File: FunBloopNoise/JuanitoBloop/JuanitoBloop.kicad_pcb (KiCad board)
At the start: 2 copper layers, 30 parts, among them J1 Trig, J2 CV, J3 Out, Q1 2N3904, Q2 2N3904, U1 NE555, U2 4046, U3 NE5532

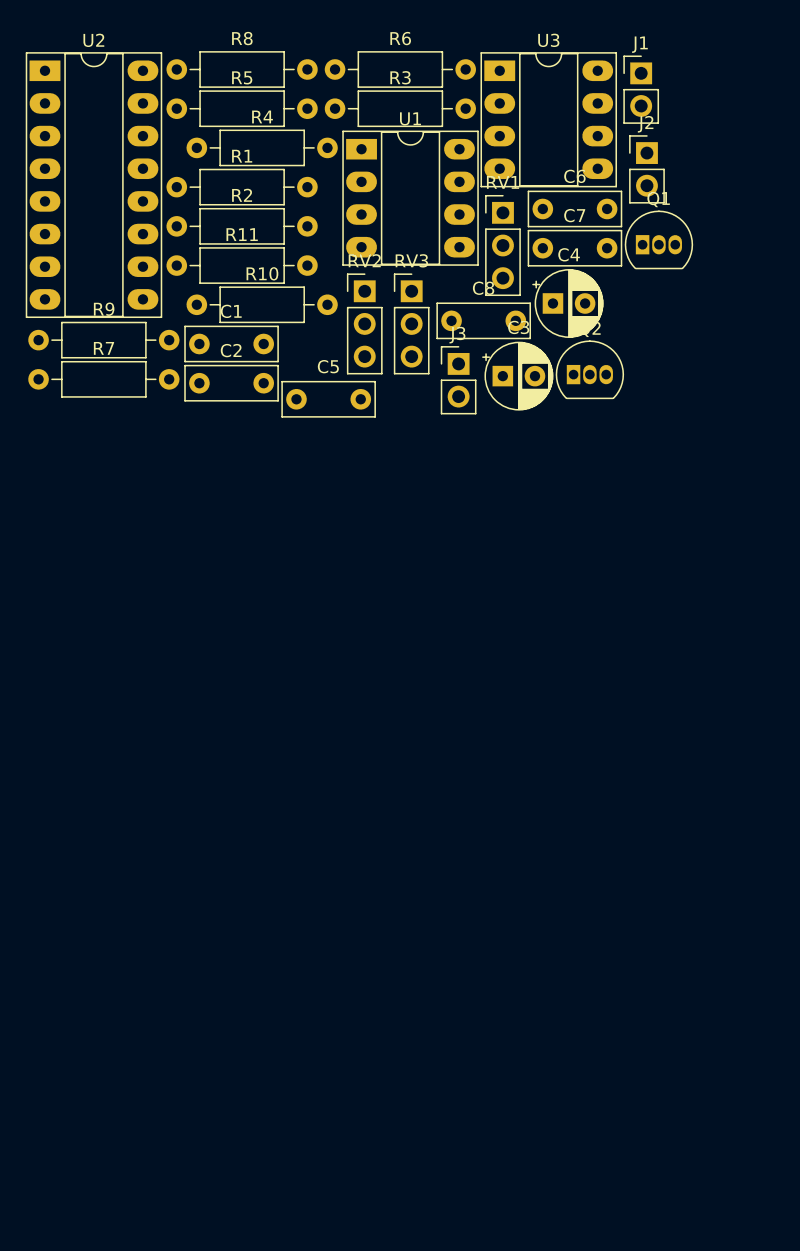
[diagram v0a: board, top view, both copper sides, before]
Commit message: schematic v2 and pcb v1
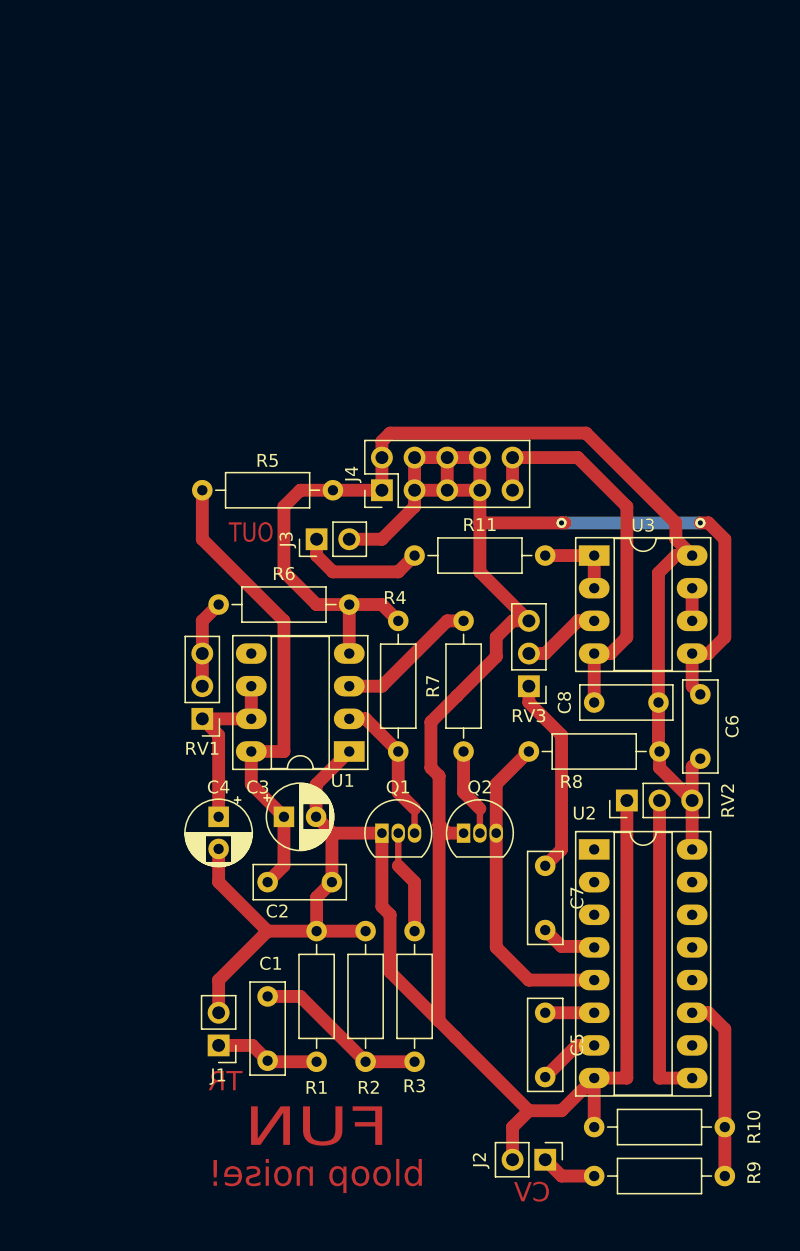
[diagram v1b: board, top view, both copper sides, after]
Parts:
- added J4: Power, Connector_PinHeader_2.54mm:PinHeader_2x05_P2.54mm_Vertical, F.Cu at (144.8, 95.2)
- moved J1 82.4 mm to (132.1, 138.4), turned to 180 degrees
- moved J2 78.7 mm to (157.5, 147.3), turned to 270 degrees
- moved R9 78.1 mm to (161.3, 148.6)
- moved R10 76.0 mm to (171.4, 144.8), turned to 180 degrees
- moved U2 74.1 mm to (161.3, 123.2)
- moved R1 68.9 mm to (139.7, 139.7), turned to 90 degrees
- moved R2 66.6 mm to (143.5, 139.7), turned to 90 degrees
- moved R8 65.0 mm to (166.4, 115.6), turned to 180 degrees
- moved R3 64.3 mm to (147.3, 129.5), turned to 270 degrees
- moved C5 51.5 mm to (157.5, 135.9), turned to 270 degrees
- moved C1 51.0 mm to (135.9, 134.6), turned to 270 degrees
- moved Q1 50.1 mm to (144.8, 121.9)
- moved C7 48.0 mm to (157.5, 124.5), turned to 270 degrees
- moved C4 47.6 mm to (132.1, 120.7), turned to 270 degrees
- moved U1 46.9 mm to (142.2, 115.6), turned to 180 degrees
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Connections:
- net Net-(C8-Pad1) renamed -12V
- C8 pad 2: Net-(C8-Pad2) -> +12V
- U3 pad 8: Net-(C8-Pad2) -> +12V
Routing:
- net GND: track 0.00 -> 216.5 mm, vias 0 -> 2
- net +12V: track 0.00 -> 89.7 mm
- net Net-(C2-Pad1): track 0.00 -> 37.2 mm
- net -12V: track 0.00 -> 30.0 mm
- net Net-(Q2-Pad3): track 0.00 -> 25.0 mm
- net Net-(RV2-Pad2): track 0.00 -> 24.1 mm
- net Net-(C7-Pad1): track 0.00 -> 15.5 mm
- net Net-(C4-Pad1): track 0.00 -> 14.5 mm
- net Net-(R10-Pad1): track 0.00 -> 14.5 mm
- net Net-(C1-Pad1): track 0.00 -> 13.5 mm
- net Net-(Q1-Pad3): track 0.00 -> 11.7 mm
- net Net-(R7-Pad2): track 0.00 -> 11.0 mm
- net Net-(J3-Pad1): track 0.00 -> 9.94 mm
- net Net-(Q1-Pad2): track 0.00 -> 8.15 mm
- net Net-(C1-Pad2): track 0.00 -> 8.15 mm
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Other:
- board text added: "CV"
- board text added: "FUN"
- board text added: "OUT"
- board text added: "TR"
- board text added: "bloop noise!"

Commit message: added ground plane, schematic documentation
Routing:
- net GND: track 216.5 -> 186.0 mm, vias 2 -> 0
- added copper zone on F.Cu, net GND
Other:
- board text added: "Bloop Noise!"
- board text removed: "bloop noise!"

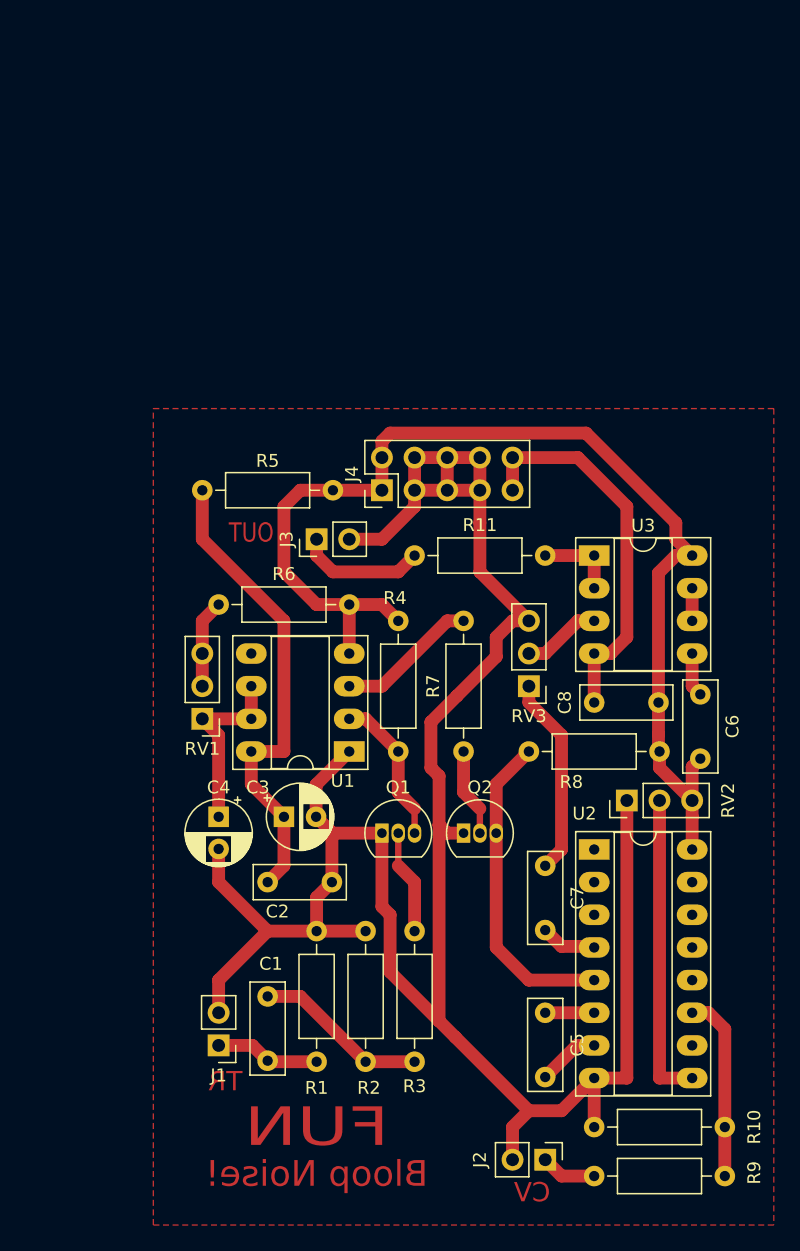
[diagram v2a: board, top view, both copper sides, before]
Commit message: switched copper layer to back
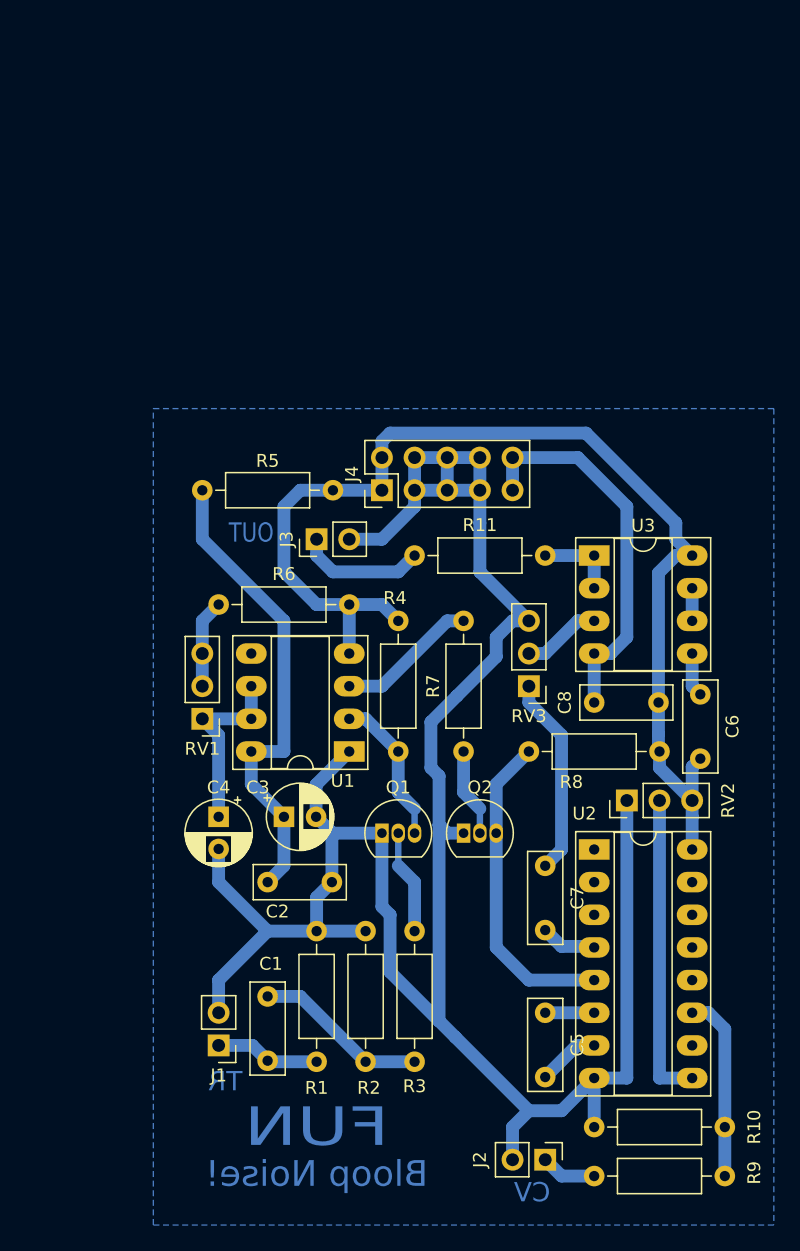
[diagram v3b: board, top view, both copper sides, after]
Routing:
- added copper zone on B.Cu, net GND
- removed copper zone on F.Cu, net GND

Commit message: tidied up print files
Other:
- board text added: "+12"
- board text added: "-12"
- board text added: "v1.0"
